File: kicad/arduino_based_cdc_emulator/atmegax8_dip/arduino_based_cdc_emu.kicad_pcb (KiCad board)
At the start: 2 copper layers, 50 x 48.3 mm, 40 parts, among them IC1 ATMEGA328-P, U1 78L05, U2 4066, U3 TL072, X1 16MHz

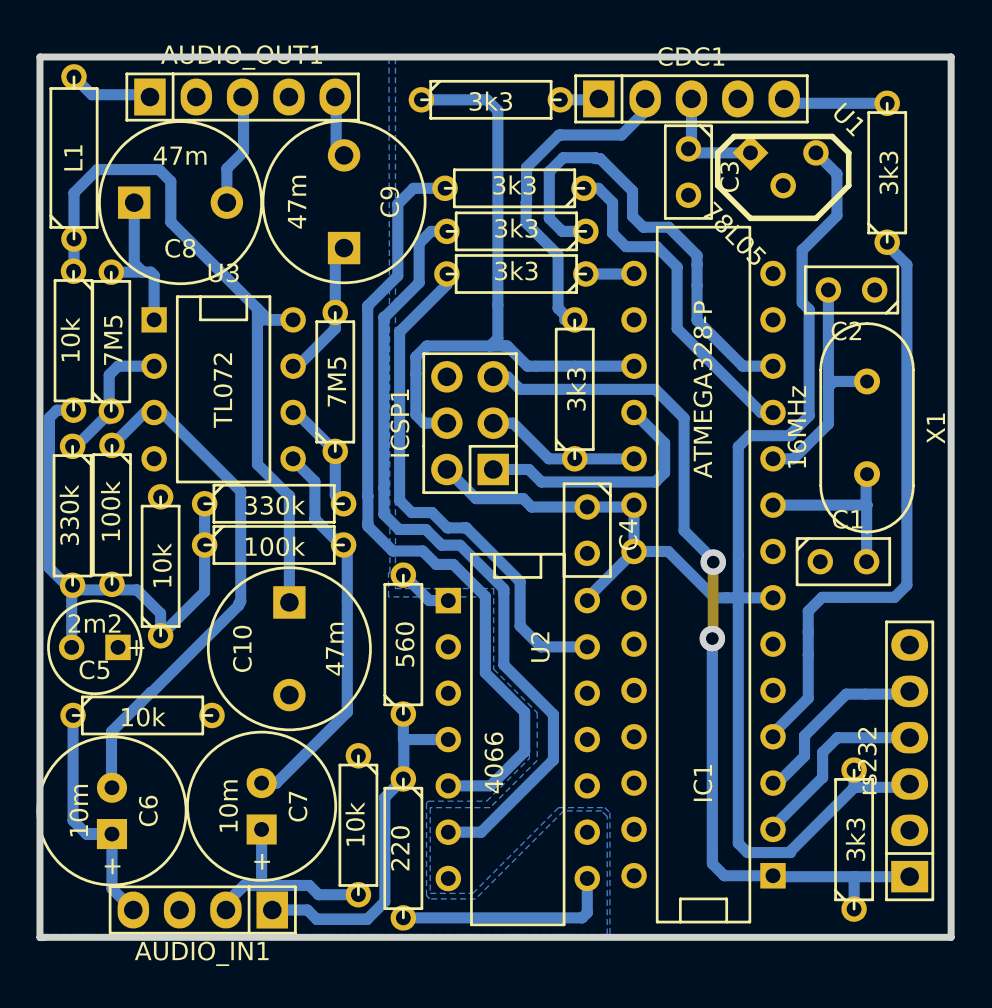
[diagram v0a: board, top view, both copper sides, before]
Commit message: 4066 powered from battery to have lower switchedON resistance then on 5V
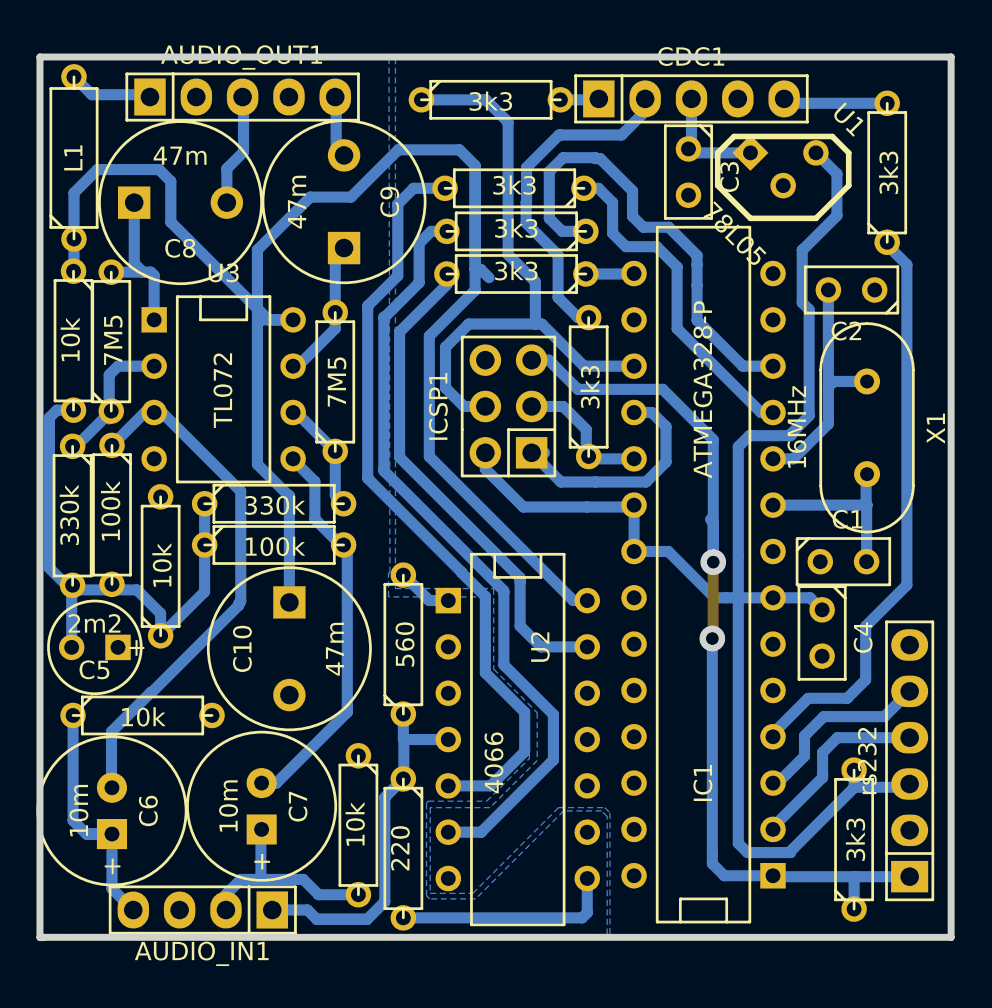
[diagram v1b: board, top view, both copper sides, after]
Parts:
- moved C4 14.1 mm to (241.6, 91.0)
- moved ICSP1 2.30 mm to (224.4, 78.6)
- moved R2 0.77 mm to (228.8, 77.5)
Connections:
- U2 pad 14: +5V -> +BATT
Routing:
- net +BATT: track 40.8 -> 94.0 mm
- net +5V: track 81.4 -> 79.3 mm
- net /MOSI: track 35.2 -> 33.6 mm
- net /PLAY: track 44.4 -> 42.9 mm
- net /NEXT: track 44.6 -> 43.1 mm
- net /PREV: track 28.7 -> 27.4 mm
- net Net-(IC1-Pad4): track 32.9 -> 31.9 mm
- net /SCK: track 8.60 -> 7.66 mm
- net /RESET: track 49.8 -> 50.7 mm
- net /LEFT IN: track 12.8 -> 11.9 mm
- net /MISO: track 13.9 -> 13.2 mm
- net /RX: track 11.0 -> 10.4 mm

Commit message: updates, I do not remember what I changed ....
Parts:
- moved R1 16.1 mm to (226.6, 77.5), turned to 90 degrees
- moved ICSP1 1.52 mm to (222.9, 78.4)
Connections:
- IC1 pad 13: (no net) -> Net-(IC1-Pad13)
- IC1 pad 15: Net-(IC1-Pad15) -> (no net)
- R1 pad 1: /MOSI -> /MISO
- R7 pad 1: Net-(IC1-Pad15) -> Net-(IC1-Pad13)
- R8 pad 1: Net-(IC1-Pad11) -> Net-(IC1-Pad12)
- R9 pad 1: Net-(IC1-Pad12) -> Net-(IC1-Pad11)
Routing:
- net Net-(IC1-Pad13): track 0.00 -> 22.3 mm
- net /MOSI: track 33.6 -> 16.4 mm
- net /DataIn: track 2.13 -> 16.1 mm
- net Net-(IC1-Pad12): track 25.4 -> 15.9 mm
- net +BATT: track 94.0 -> 85.8 mm
- net Net-(IC1-Pad15): track 2.91 -> 0.00 mm
- net /PLAY: track 42.9 -> 40.9 mm
- net +5V: track 79.3 -> 81.1 mm
- net /MISO: track 13.2 -> 14.9 mm
- net Net-(IC1-Pad11): track 18.5 -> 16.9 mm
- net /SCK: track 7.66 -> 9.22 mm
- net /NEXT: track 43.1 -> 41.6 mm
- net /RESET: track 50.7 -> 49.9 mm
- net /Clock: track 18.5 -> 17.7 mm
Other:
- net class Default: trace_width 0.6096 -> 0.5
